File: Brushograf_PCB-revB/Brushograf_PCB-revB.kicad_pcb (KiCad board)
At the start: 2 copper layers, 198 x 48 mm, 49 parts, among them J1 Conn_01x05_Socket, J2 Conn_01x05_Socket, J3 Conn_01x05_Socket, J5 Barrel_Jack_Switch, J6 Conn_01x07_Socket, J7 Conn_01x03_Pin, J8 SD_CARD_MICRO_AMPHENOL_114008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, Q1 AO3401A, U1 ULN2003A, U2 ULN2003A, U3 ULN2003A, U4 ESP32-DevKitC

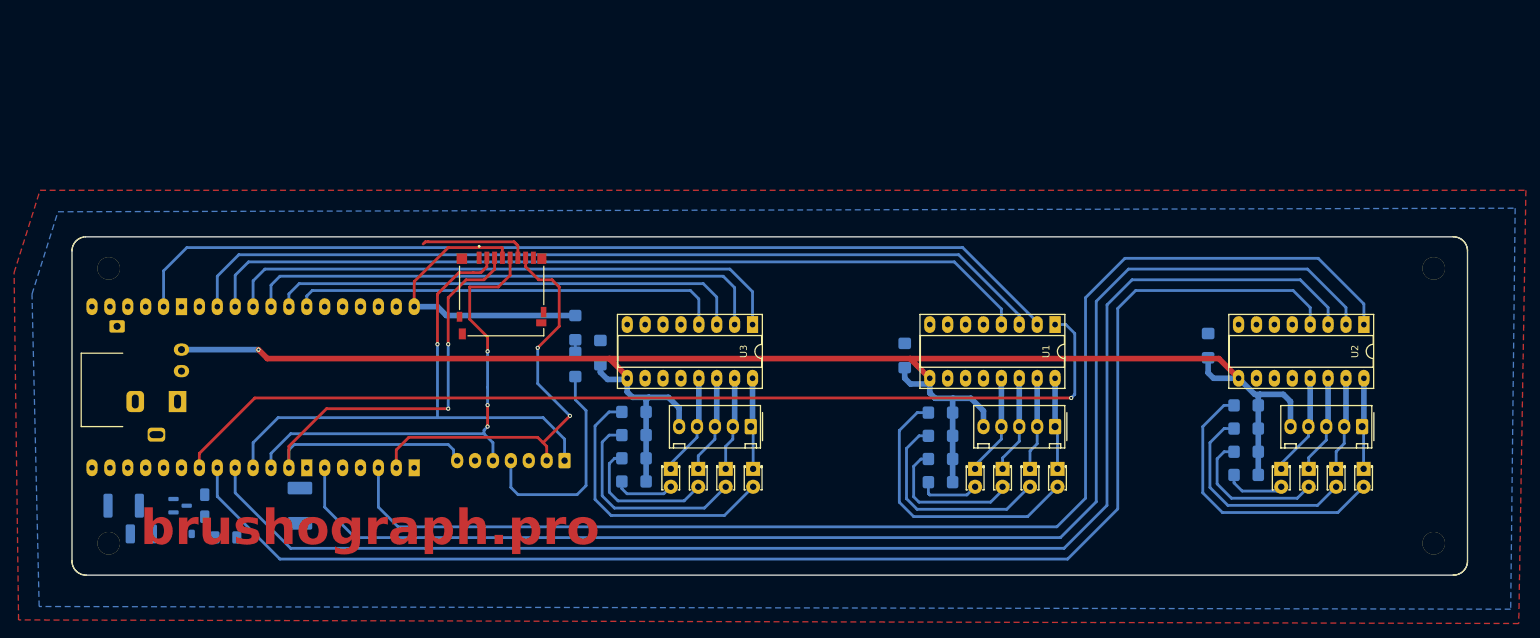
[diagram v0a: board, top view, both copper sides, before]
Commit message: USB-C as the only inlet; lever switch and RJ-12 placed on the board edges
Grows the outline 25mm along the top (198x48 -> 198x73mm) and places every
new part. The RJ-12 needs ~19mm behind the top edge and the old board had
11mm before the back-side SPI tracks, which is what forced the growth.
Everything from rev A keeps its coordinates.

  - The barrel jack is now gone, with its reverse-polarity FET, zener and
    gate resistor. USB-C is the sole power inlet: VBUS through a 1.5A
    polyfuse straight to the rail feeding both converters.
  - J12 sits on the left edge, receptacle overhanging it.
  - SW1 becomes an NKK GW12L panel lever switch on the left edge with the
    actuator overhanging, replacing the DIP slide. It is a 1P2T used as a
    break: common to the ESP32, one throw to the board 5V, the other open.
  - J13 RJ-12 sits on the upper edge, opening facing off the board.

Copper pours are grown with the outline and refilled, so the new strip is
poured rather than stopping partway up it.

Placement was validated against a 0.25mm occupancy model of the existing
copper, and every non-J12 DRC error is inherited unchanged from rev A.

J12 reports 27 shorting_items and 4 hole_clearance errors that are NOT
caused by the placement: the same 31 appear with the untouched stock
footprint alone on an empty board. The pads have real 0.2-0.7mm gaps and
nothing bridges them; zones, solder mask and neighbouring copper were each
ruled out by experiment, and every USB-C footprint in the KiCad library has
sub-0.25mm pad gaps. Flagged in the README to look at in the GUI.

53 ratsnest connections remain to be routed.

Co-Authored-By: Claude Opus 5 <noreply@anthropic.com>
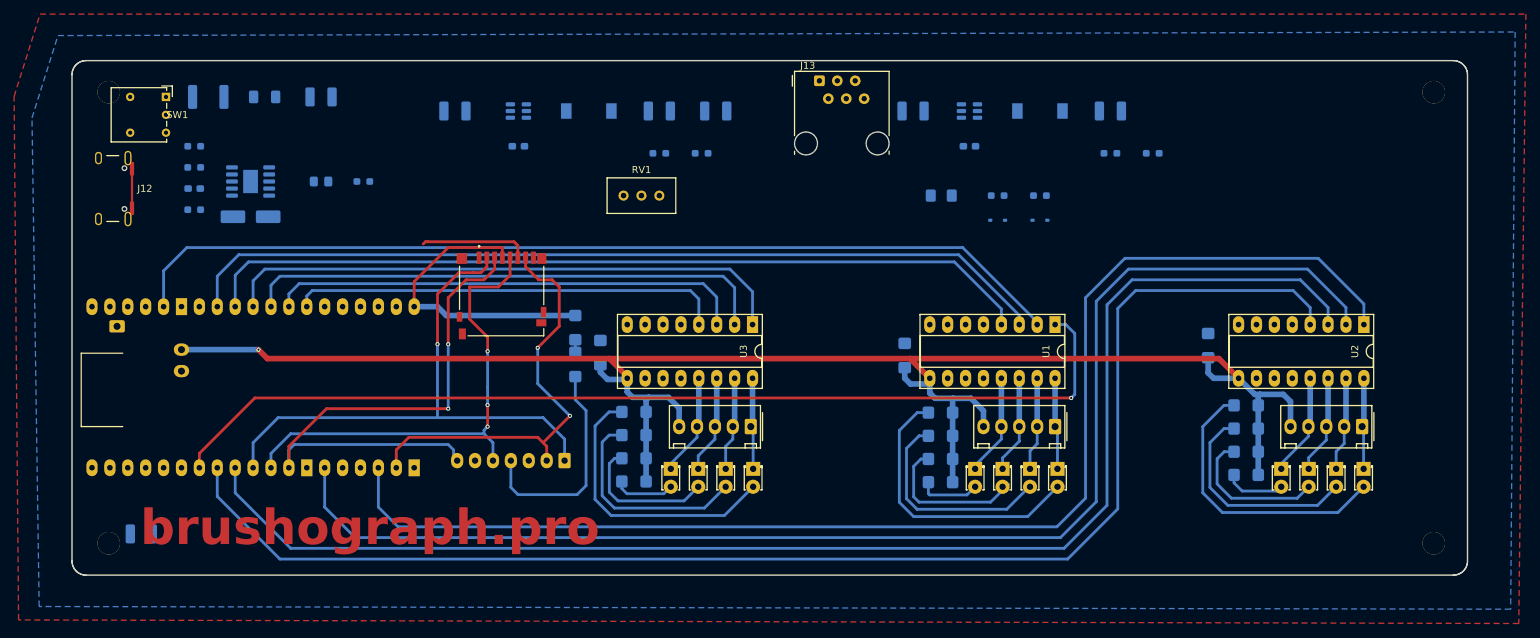
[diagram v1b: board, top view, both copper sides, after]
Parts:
- removed D13: BZX84C10, Diode_SMD:D_SOD-123
- removed J5: Barrel_Jack_Switch, Connector_BarrelJack:BarrelJack_Horizontal
- removed Q1: AO3401A, Package_TO_SOT_SMD:SOT-23
- removed R21: 100k, Resistor_SMD:R_1206_3216Metric_Pad1.30x1.75mm_HandSolder
- added C10: 22uF/35V, Capacitor_SMD:C_1210_3225Metric_Pad1.33x2.70mm_HandSolder, B.Cu at (80.0, 66.0)
- added C11: 10uF/35V, Capacitor_SMD:C_1210_3225Metric_Pad1.33x2.70mm_HandSolder, B.Cu at (99.0, 68.0)
- added C12: 100nF, Capacitor_SMD:C_0603_1608Metric_Pad1.08x0.95mm_HandSolder, B.Cu at (108.0, 73.0)
- added C13: 22uF/25V, Capacitor_SMD:C_1210_3225Metric_Pad1.33x2.70mm_HandSolder, B.Cu at (128.0, 68.0)
- added C14: 22uF/25V, Capacitor_SMD:C_1210_3225Metric_Pad1.33x2.70mm_HandSolder, B.Cu at (136.0, 68.0)
- added C15: 10uF/35V, Capacitor_SMD:C_1210_3225Metric_Pad1.33x2.70mm_HandSolder, B.Cu at (164.0, 68.0)
- added C16: 100nF, Capacitor_SMD:C_0603_1608Metric_Pad1.08x0.95mm_HandSolder, B.Cu at (172.0, 73.0)
- added C17: 22uF/25V, Capacitor_SMD:C_1210_3225Metric_Pad1.33x2.70mm_HandSolder, B.Cu at (192.0, 68.0)
- added C9: 1uF, Capacitor_SMD:C_0603_1608Metric_Pad1.08x0.95mm_HandSolder, B.Cu at (62.0, 79.0)
- added D17: PD OK, LED_SMD:LED_0805_2012Metric_Pad1.15x1.40mm_HandSolder, B.Cu at (80.0, 78.0)
- added D18: PESD5V0S1BA, Diode_SMD:D_SOD-323, B.Cu at (176.0, 83.5)
- added D19: PESD5V0S1BA, Diode_SMD:D_SOD-323, B.Cu at (182.0, 83.5)
- added F2: 0.5A, Fuse:Fuse_1206_3216Metric_Pad1.42x1.75mm_HandSolder, B.Cu at (168.0, 80.0)
- added J12: USB-C PD in, Connector_USB:USB_C_Receptacle_GCT_USB4105-xx-A_16P_TopMnt_Horizontal, F.Cu at (49.5, 79.0)
- added J13: Pendant, Connector_RJ:RJ12_Amphenol_54601-x06_Horizontal, F.Cu at (150.7, 63.7)
- added L1: 10uH 3.5A, Inductor_SMD:L_7.3x7.3_H4.5, B.Cu at (118.0, 68.0)
- added L2: 15uH 2A, Inductor_SMD:L_7.3x7.3_H4.5, B.Cu at (182.0, 68.0)
- added R22: 5.1k, Resistor_SMD:R_0603_1608Metric_Pad0.98x0.95mm_HandSolder, B.Cu at (62.0, 73.0)
- added R23: 5.1k, Resistor_SMD:R_0603_1608Metric_Pad0.98x0.95mm_HandSolder, B.Cu at (62.0, 76.0)
- added R24: 6.8k, Resistor_SMD:R_0603_1608Metric_Pad0.98x0.95mm_HandSolder, B.Cu at (62.0, 82.0)
- added R25: 1k, Resistor_SMD:R_0603_1608Metric_Pad0.98x0.95mm_HandSolder, B.Cu at (86.0, 78.0)
- added R26: 100k, Resistor_SMD:R_0603_1608Metric_Pad0.98x0.95mm_HandSolder, B.Cu at (128.0, 74.0)
- added R27: 7.5k, Resistor_SMD:R_0603_1608Metric_Pad0.98x0.95mm_HandSolder, B.Cu at (134.0, 74.0)
- added R28: 75k, Resistor_SMD:R_0603_1608Metric_Pad0.98x0.95mm_HandSolder, B.Cu at (192.0, 74.0)
- added R29: 10k, Resistor_SMD:R_0603_1608Metric_Pad0.98x0.95mm_HandSolder, B.Cu at (198.0, 74.0)
- added R30: 330, Resistor_SMD:R_0603_1608Metric_Pad0.98x0.95mm_HandSolder, B.Cu at (176.0, 80.0)
- added R31: 330, Resistor_SMD:R_0603_1608Metric_Pad0.98x0.95mm_HandSolder, B.Cu at (182.0, 80.0)
- added RV1: 10k, Potentiometer_THT:Potentiometer_Bourns_3296W_Vertical, F.Cu at (128.0, 80.0)
- added SW1: ESP POWER, Button_Switch_THT:SW_Lever_1P2T_NKK_GW12LxH, F.Cu at (58.0, 66.0)
- added U6: CH224K, Package_SO:SSOP-10-1EP_3.9x4.9mm_P1mm_EP2.1x3.3mm, B.Cu at (70.0, 78.0)
- added U7: TPS54202, Package_TO_SOT_SMD:SOT-23-6, B.Cu at (108.0, 68.0)
- added U8: TPS54202, Package_TO_SOT_SMD:SOT-23-6, B.Cu at (172.0, 68.0)
- C7: value 10uF/50V -> 10uF/35V
- moved F1 59.2 mm to (64.0, 66.0)
- moved C7 58.6 mm to (72.0, 66.0), turned to 0 degrees
- moved D14 41.6 mm to (70.0, 83.0), turned to 0 degrees
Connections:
- C7 pad 1: VIN_DC -> VSUP
- F1 pad 1: VIN -> VBUS
- F1 pad 2: Net-(Q1-D) -> VSUP
- U4 pad 3: LIM_Z -> unconnected-(U4-SENSOR_VP/GPIO36/ADC1_CH0-Pad3)
- U4 pad 5: LIM_X -> unconnected-(U4-VDET_1/GPIO34/ADC1_CH6-Pad5)
- U4 pad 6: LIM_Y -> unconnected-(U4-VDET_2/GPIO35/ADC1_CH7-Pad6)
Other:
- board size 198 x 48 mm -> 198 x 73 mm
